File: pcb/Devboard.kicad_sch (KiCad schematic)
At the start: 36 parts, among them J1 USB_C_Receptacle_USB2.0_14P, J2 Conn_01x20, J3 Conn_01x20, J4 Conn_01x03, SW1 SW_Push, U1 RP2040, U2 NCP1117-3.3_SOT223, U3 W25Q128JVS, Y1 12 MHz

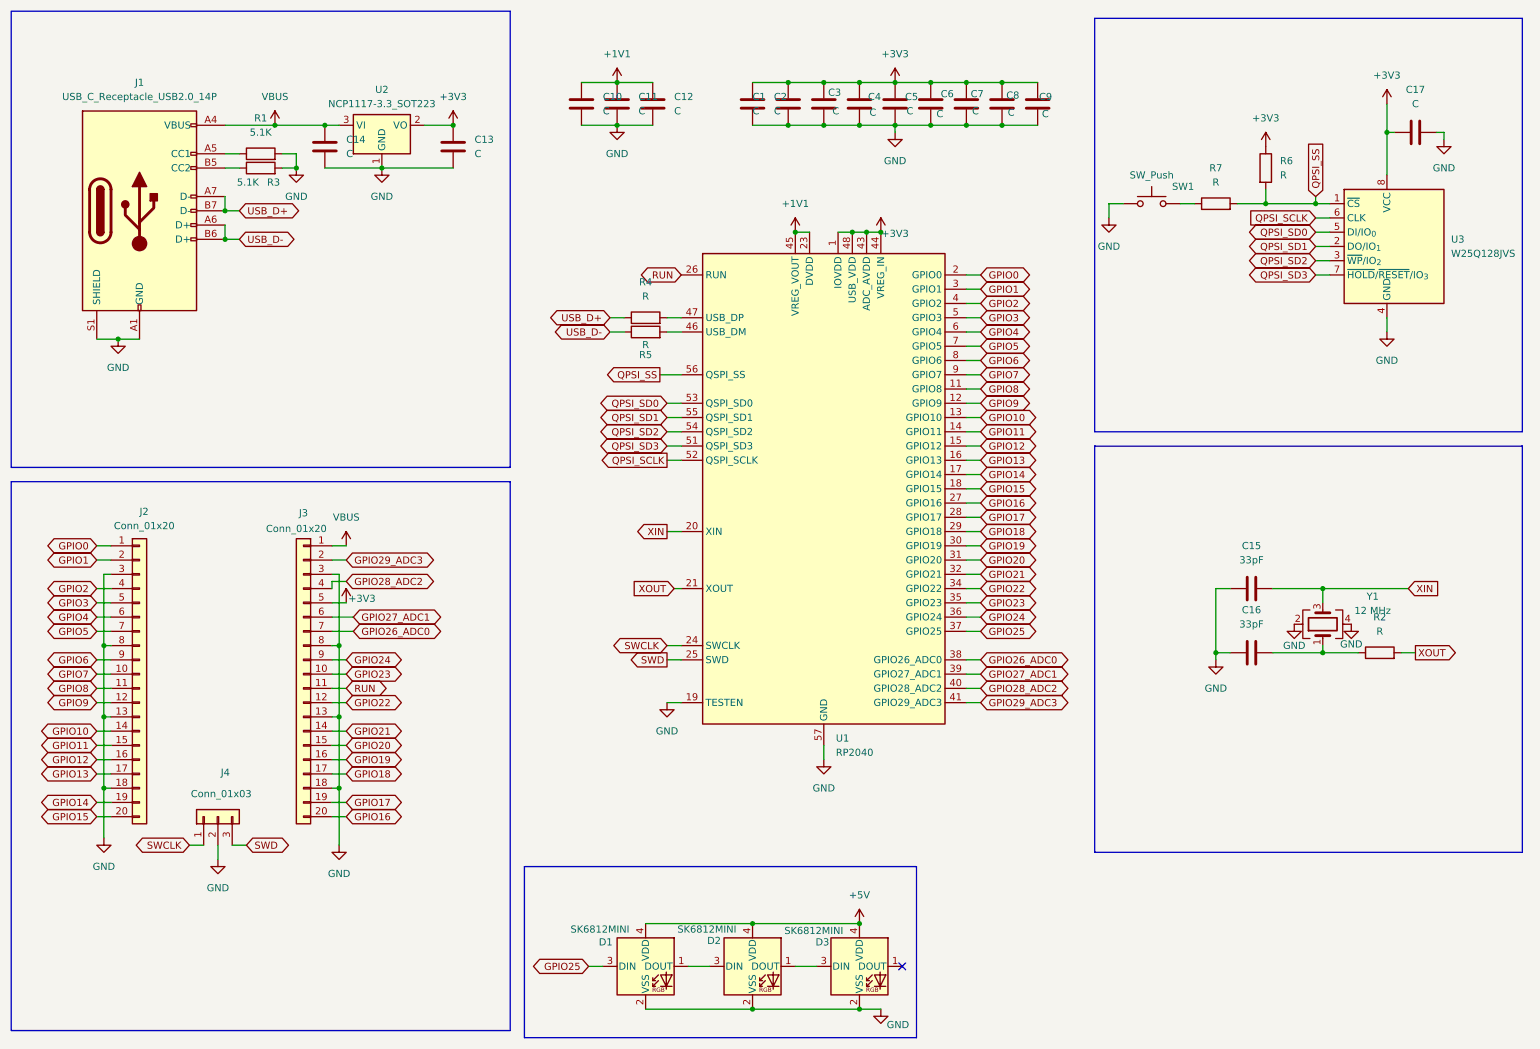
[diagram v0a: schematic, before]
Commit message: added bom
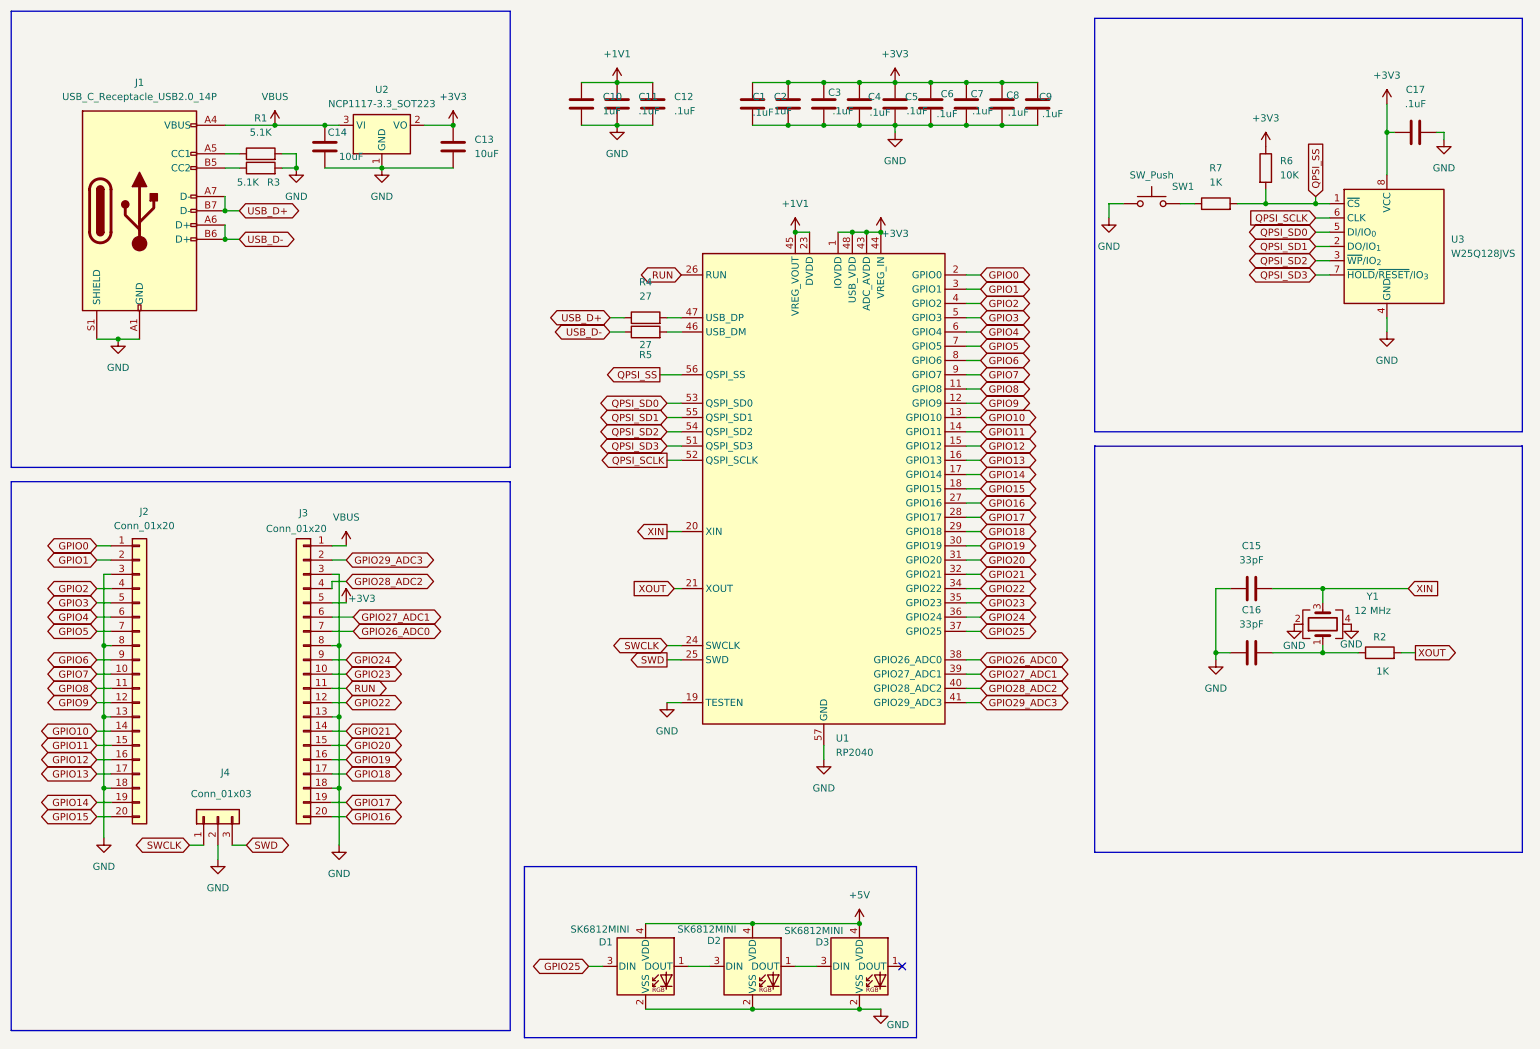
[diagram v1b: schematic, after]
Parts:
- C1, C11, C12, C17, C3, C4, C5, C6, C7, C8, C9: value C -> .1uF
- C10, C2: value C -> 1uF
- C13, C14: value C -> 10uF
- R2, R7: value R -> 1K
- R4, R5: value R -> 27
- R6: value R -> 10K
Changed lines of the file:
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@@
 			)
 		)
-		(property "Value" "C"
+		(property "Value" ".1uF"
 			(at 132.08 31.7499 0)
 			(effects
@@
 			)
 		)
-		(property "Value" "C"
+		(property "Value" "1uF"
 			(at 149.86 31.7499 0)
 			(effects
@@
 			)
 		)
-		(property "Value" "C"
+		(property "Value" ".1uF"
 			(at 191.516 32.004 0)
 			(effects
@@
 			)
 		)
-		(property "Value" "R"
+		(property "Value" "10K"
 			(at 240.03 43.1799 0)
 			(effects
@@
 			)
 		)
-		(property "Value" "C"
+		(property "Value" ".1uF"
 			(at 166.878 32.004 0)
 			(effects
@@
 		(on_board yes)
 		(dnp no)
-		(fields_autoplaced yes)
 		(property "Reference" "R2"
-			(at 257.81 121.92 90)
+			(at 257.81 125.476 90)
 			(effects
 				(font
@@
 			)
 		)
-		(property "Value" "R"
-			(at 257.81 124.46 90)
+		(property "Value" "1K"
+			(at 258.318 131.572 90)
 			(effects
 				(font
@@
 			)
 		)
-		(property "Value" "C"
+		(property "Value" ".1uF"
 			(at 178.816 32.258 0)
 			(effects
@@
 			)
 		)
-		(property "Value" "C"
-			(at 146.05 31.7499 0)
+		(property "Value" ".1uF"
+			(at 146.05 32.004 0)
 			(effects
 				(font
@@
 			)
 		)
-		(property "Value" "C"
+		(property "Value" ".1uF"
 			(at 185.166 31.75 0)
 			(effects
@@
 			)
 		)
-		(property "Value" "C"
+		(property "Value" ".1uF"
 			(at 173.482 31.75 0)
 			(effects
@@
 			)
 		)
-		(property "Value" "C"
+		(property "Value" "10uF"
 			(at 96.52 39.3699 0)
 			(effects
@@
 			)
 		)
-		(property "Value" "C"
+		(property "Value" ".1uF"
 			(at 125.73 31.7499 0)
 			(effects
@@
 			)
 		)
-		(property "Value" "C"
+		(property "Value" ".1uF"
 			(at 264.16 30.48 90)
 			(effects
@@
 			)
 		)
-		(property "Value" "R"
+		(property "Value" "27"
 			(at 127 73.406 90)
 			(effects
@@
 		(on_board yes)
 		(dnp no)
-		(fields_autoplaced yes)
 		(property "Reference" "C14"
-			(at 73.66 36.8299 0)
+			(at 70.358 35.56 0)
 			(effects
 				(font
@@
 			)
 		)
-		(property "Value" "C"
-			(at 73.66 39.3699 0)
+		(property "Value" "10uF"
+			(at 72.39 39.878 0)
 			(effects
 				(font
@@
 			)
 		)
-		(property "Value" "C"
+		(property "Value" ".1uF"
 			(at 160.274 31.75 0)
 			(effects
@@
 			)
 		)
-		(property "Value" "R"
+		(property "Value" "1K"
 			(at 228.6 44.45 90)
 			(effects
@@
 			)
 		)
-		(property "Value" "C"
+		(property "Value" "1uF"
 			(at 119.38 31.7499 0)
 			(effects
@@
 			)
 		)
-		(property "Value" "C"
+		(property "Value" ".1uF"
 			(at 197.612 32.258 0)
 			(effects
@@
 			)
 		)
-		(property "Value" "R"
+		(property "Value" "27"
 			(at 127 64.77 90)
 			(effects

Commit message: updated routing
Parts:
- removed U2: NCP1117-3.3_SOT223, Package_TO_SOT_SMD:SOT-223-3_TabPin2, symbol Regulator_Linear:NCP1117-3.3_SOT223
- removed U3: W25Q128JVS, Package_SO:SOIC-8_5.3x5.3mm_P1.27mm, symbol Memory_Flash:W25Q128JVS
- added U2: MCP1700x-330xxTT, Package_TO_SOT_SMD:SOT-23, symbol Regulator_Linear:MCP1700x-330xxTT
- added U3: W25Q16JVSS, Package_SON:Winbond_USON-8-1EP_3x2mm_P0.5mm_EP0.2x1.6mm, symbol Memory_Flash:W25Q16JVSS
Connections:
- net +3V3: now also U2.2 (VO), U3.8 (VCC)
- net GND: now also U2.1 (GND), U3.4 (GND)
- net QPSI_SCLK: now also U3.6 (CLK)
- net QPSI_SD0: now also U3.5 (DI/IO_{0})
- net QPSI_SD1: now also U3.2 (DO/IO_{1})
- net QPSI_SD2: now also U3.3 (~{WP}/IO_{2})
- net QPSI_SD3: now also U3.7 (~{HOLD}/~{RESET}/IO_{3})
- net QPSI_SS: now also U3.1 (~{CS})
- net VBUS: now also U2.3 (VI)
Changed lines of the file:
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@@
+	)
+	(symbol
+		(lib_id "Memory_Flash:W25Q16JVSS")
+		(at 259.08 55.88 0)
+		(unit 1)
+		(exclude_from_sim no)
+		(in_bom yes)
+		(on_board yes)
+		(dnp no)
+		(fields_autoplaced yes)
+		(property "Reference" "U3"
+			(at 270.51 54.6099 0)
+			(effects
+				(font
+					(size 1.27 1.27)
+				)
+				(justify left)
+			)
+		)
+		(property "Value" "W25Q16JVSS"
+			(at 270.51 57.1499 0)
+			(effects
+				(font
+					(size 1.27 1.27)
+				)
+				(justify left)
+			)
+		)
+		(property "Footprint" "Package_SON:Winbond_USON-8-1EP_3x2mm_P0.5mm_EP0.2x1.6mm"
+			(at 259.08 55.88 0)
+			(effects
+				(font
+					(size 1.27 1.27)
+				)
+				(hide yes)
+			)
+		)
+		(property "Datasheet" "https://www.winbond.com/hq/support/documentation/levelOne.jsp?__locale=en&DocNo=DA00-W25Q16JV.1"
+			(at 259.08 55.88 0)
+			(effects
+				(font
+					(size 1.27 1.27)
+				)
+				(hide yes)
+			)
+		)
+		(property "Description" "16Mbit / 2MiB Serial Flash Memory, Standard/Dual/Quad SPI, 2.7-3.6V, SOIC-8 (208 mil)"
+			(at 259.08 55.88 0)
+			(effects
+				(font
+					(size 1.27 1.27)
+				)
+				(hide yes)
+			)
+		)
+		(pin "6"
+		)
+		(pin "8"
+		)
+		(pin "5"
+		)
+		(pin "2"
+		)
+		(pin "1"
+		)
+		(pin "3"
+		)
+		(pin "7"
+		)
+		(pin "4"
+		)
+		(instances
+			(project ""
+				(path "/9334ac6d-09d4-488c-a185-71def342f1a6"
+					(reference "U3")
+					(unit 1)
+				)
+			)
+		)
 	)
 	(symbol
@@
 	)
 	(symbol
+		(lib_id "Regulator_Linear:MCP1700x-330xxTT")
+		(at 80.01 34.29 0)
+		(unit 1)
+		(exclude_from_sim no)
+		(in_bom yes)
+		(on_board yes)
+		(dnp no)
+		(fields_autoplaced yes)
+		(property "Reference" "U2"
+			(at 80.01 27.94 0)
+			(effects
+				(font
+					(size 1.27 1.27)
+				)
+			)
+		)
+		(property "Value" "MCP1700x-330xxTT"
+			(at 80.01 30.48 0)
+			(effects
+				(font
+					(size 1.27 1.27)
+				)
+			)
+		)
+		(property "Footprint" "Package_TO_SOT_SMD:SOT-23"
+			(at 80.01 28.575 0)
+			(effects
+				(font
+					(size 1.27 1.27)
+				)
+				(hide yes)
+			)
+		)
+		(property "Datasheet" "http://ww1.microchip.com/downloads/en/DeviceDoc/20001826D.pdf"
+			(at 80.01 34.29 0)
+			(effects
+				(font
+					(size 1.27 1.27)
+				)
+				(hide yes)
+			)
+		)
+		(property "Description" "250mA Low Quiscent Current LDO, 3.3V output, SOT-23"
+			(at 80.01 34.29 0)
+			(effects
+				(font
+					(size 1.27 1.27)
+				)
+				(hide yes)
+			)
+		)
+		(pin "3"
+		)
+		(pin "1"
+		)
+		(pin "2"
+		)
+		(instances
+			(project ""
+				(path "/9334ac6d-09d4-488c-a185-71def342f1a6"
+					(reference "U2")
+					(unit 1)
+				)
+			)
+		)
+	)
+	(symbol
 		(lib_id "power:+3V3")
 		(at 92.71 34.29 0)
@@
 	)
 	(symbol
-		(lib_id "Memory_Flash:W25Q128JVS")
-		(at 259.08 55.88 0)
-		(unit 1)
-		(exclude_from_sim no)
-		(in_bom yes)
-		(on_board yes)
-		(dnp no)
-		(fields_autoplaced yes)
-		(property "Reference" "U3"
-			(at 270.51 54.6099 0)
-			(effects
-				(font
-					(size 1.27 1.27)
-				)
-				(justify left)
-			)
-		)
-		(property "Value" "W25Q128JVS"
-			(at 270.51 57.1499 0)
-			(effects
-				(font
-					(size 1.27 1.27)
-				)
-				(justify left)
-			)
-		)
-		(property "Footprint" "Package_SO:SOIC-8_5.3x5.3mm_P1.27mm"
-			(at 259.08 33.02 0)
-			(effects
-				(font
-					(size 1.27 1.27)
-				)
-				(hide yes)
-			)
-		)
-		(property "Datasheet" "https://www.winbond.com/resource-files/w25q128jv_dtr%20revc%2003272018%20plus.pdf"
-			(at 259.08 30.48 0)
-			(effects
-				(font
-					(size 1.27 1.27)
-				)
-				(hide yes)
-			)
-		)
-		(property "Description" "128Mbit / 16MiB Serial Flash Memory, Standard/Dual/Quad SPI, 2.7-3.6V, SOIC-8"
-			(at 259.08 27.94 0)
-			(effects
-				(font
-					(size 1.27 1.27)
-				)
-				(hide yes)
-			)
-		)
-		(pin "5"
-		)
-		(pin "4"
-		)
-		(pin "8"
-		)
-		(pin "6"
-		)
-		(pin "1"
-		)
-		(pin "2"
-		)
-		(pin "3"
-		)
-		(pin "7"
-		)
-		(instances
-			(project ""
-				(path "/9334ac6d-09d4-488c-a185-71def342f1a6"
-					(reference "U3")
-					(unit 1)
-				)
-			)
-		)
-	)
-	(symbol
 		(lib_id "Device:C")
 		(at 121.92 30.48 0)
@@
 					(unit 1)
 				)
-			)
-		)
-	)
-	(symbol
-		(lib_id "Regulator_Linear:NCP1117-3.3_SOT223")
-		(at 80.01 34.29 0)
-		(unit 1)
-		(exclude_from_sim no)
-		(in_bom yes)
-		(on_board yes)
-		(dnp no)
-		(fields_autoplaced yes)
-		(property "Reference" "U2"
-			(at 80.01 27.94 0)
-			(effects
-				(font
-					(size 1.27 1.27)
-				)
-			)
-		)
-		(property "Value" "NCP1117-3.3_SOT223"
-			(at 80.01 30.48 0)
-			(effects
-				(font
-					(size 1.27 1.27)
-				)
-			)
-		)
-		(property "Footprint" "Package_TO_SOT_SMD:SOT-223-3_TabPin2"
-			(at 80.01 29.21 0)
-			(effects
-				(font
-					(size 1.27 1.27)
-				)
-				(hide yes)
-			)
-		)
-		(property "Datasheet" "http://www.onsemi.com/pub_link/Collateral/NCP1117-D.PDF"
-			(at 82.55 40.64 0)
-			(effects
-				(font
-					(size 1.27 1.27)
-				)
-				(hide yes)
-			)
-		)
-		(property "Description" "1A Low drop-out regulator, Fixed Output 3.3V, SOT-223"
-			(at 80.01 34.29 0)
-			(effects
-				(font
-					(size 1.27 1.27)
-				)
-				(hide yes)
-			)
-		)
-		(pin "3"
-		)
-		(pin "1"
-		)
-		(pin "2"
-		)
-		(instances
-			(project ""
-				(path "/9334ac6d-09d4-488c-a185-71def342f1a6"
-					(reference "U2")
-					(unit 1)
-				)
